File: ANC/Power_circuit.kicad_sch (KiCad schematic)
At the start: 16 parts, among them J2 Screw_Terminal_01x02, J4 Conn_01x04, J6 Conn_01x06, U10 LD39015M12R, U8 LD1117S12TR_SOT223, U9 LD39015M18R

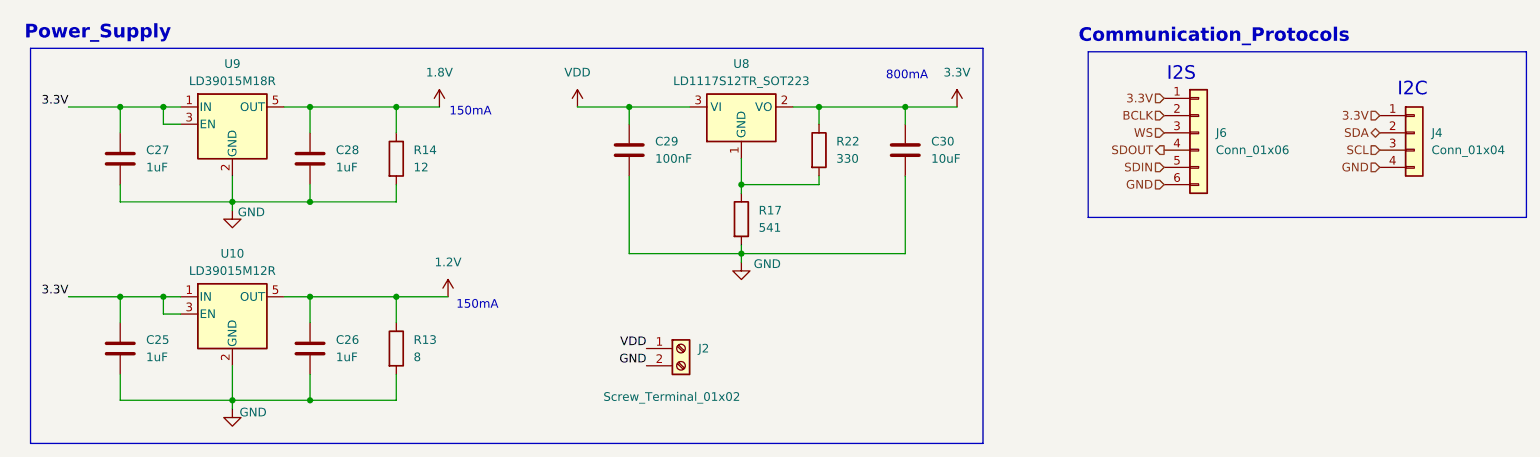
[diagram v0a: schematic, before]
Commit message: Added ANC
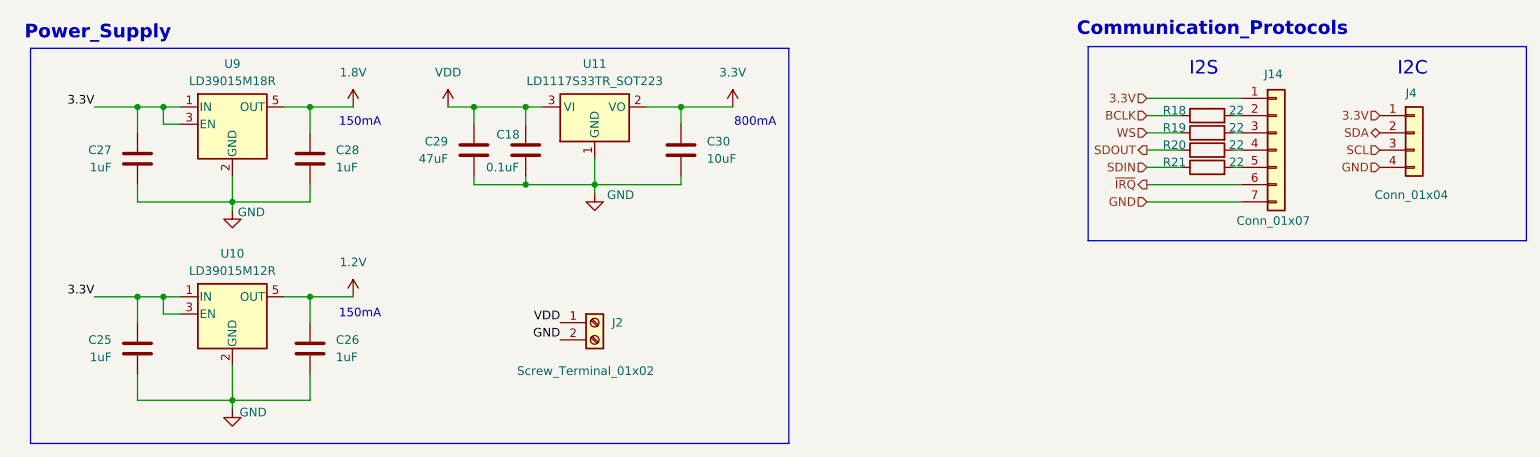
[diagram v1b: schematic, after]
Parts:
- removed J6: Conn_01x06, Connector_PinHeader_2.54mm:PinHeader_1x06_P2.54mm_Vertical, symbol Connector_Generic:Conn_01x06
- removed R13: 8, Resistor_SMD:R_0402_1005Metric_Pad0.72x0.64mm_HandSolder, symbol Device:R
- removed R14: 12, Resistor_SMD:R_0402_1005Metric_Pad0.72x0.64mm_HandSolder, symbol Device:R
- removed R17: 541, Resistor_SMD:R_0402_1005Metric_Pad0.72x0.64mm_HandSolder, symbol Device:R
- removed R22: 330, Resistor_SMD:R_0402_1005Metric_Pad0.72x0.64mm_HandSolder, symbol Device:R
- removed U8: LD1117S12TR_SOT223, Package_TO_SOT_SMD:SOT-223-3_TabPin2, symbol Regulator_Linear:LD1117S12TR_SOT223
- added C18: 0.1uF, Capacitor_SMD:C_0402_1005Metric_Pad0.74x0.62mm_HandSolder, symbol Device:C
- added J14: Conn_01x07, Connector_PinHeader_2.54mm:PinHeader_1x07_P2.54mm_Vertical, symbol Connector_Generic:Conn_01x07
- added R18, R19, R20, R21: 22, Resistor_SMD:R_0402_1005Metric_Pad0.72x0.64mm_HandSolder, symbol Device:R
- added U11: LD1117S33TR_SOT223, Package_TO_SOT_SMD:SOT-223-3_TabPin2, symbol Regulator_Linear:LD1117S33TR_SOT223
- C25, C26, C27, C28: footprint Capacitor_SMD:C_0805_2012Metric_Pad1.18x1.45mm_HandSolder -> Capacitor_SMD:C_0402_1005Metric_Pad0.74x0.62mm_HandSolder
- C29: value 100nF -> 47uF
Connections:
- net 3.3V: now also J14.1 (Pin_1), U11.2 (VO)
- net BCLK: now also R18.1
- net GND: now also C18.1, J14.7 (Pin_7), U11.1 (GND)
- net SDIN: now also R21.1
- net SDOUT: now also R20.1
- net VDD: now also C18.2, U11.3 (VI)
- net WS: now also R19.1
- new net: J14.2 (Pin_2), R18.2
- new net: J14.3 (Pin_3), R19.2
- new net: J14.4 (Pin_4), R20.2
- new net: J14.5 (Pin_5), R21.2
- new net ~{IRQ}: J14.6 (Pin_6)
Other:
- moved on the sheet: C25, C27, C29, C30, J2
